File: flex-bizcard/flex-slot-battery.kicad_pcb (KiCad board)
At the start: 2 copper layers, 71.9 x 26.5 mm, 8 parts, among them J1 Conn_01x01_Female, J2 Conn_01x01_Female, J3 Conn_01x01_Female

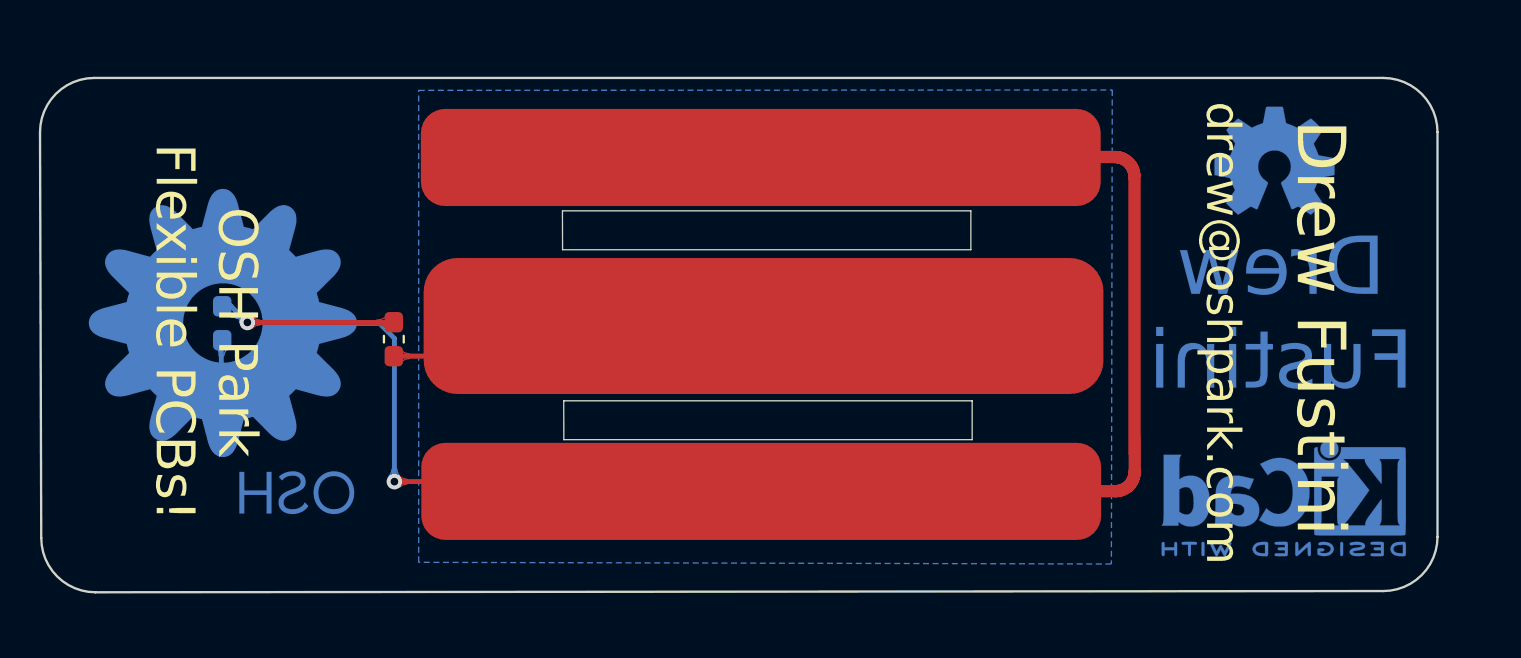
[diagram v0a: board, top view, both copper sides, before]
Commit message: add polarity mark to flex coin slot
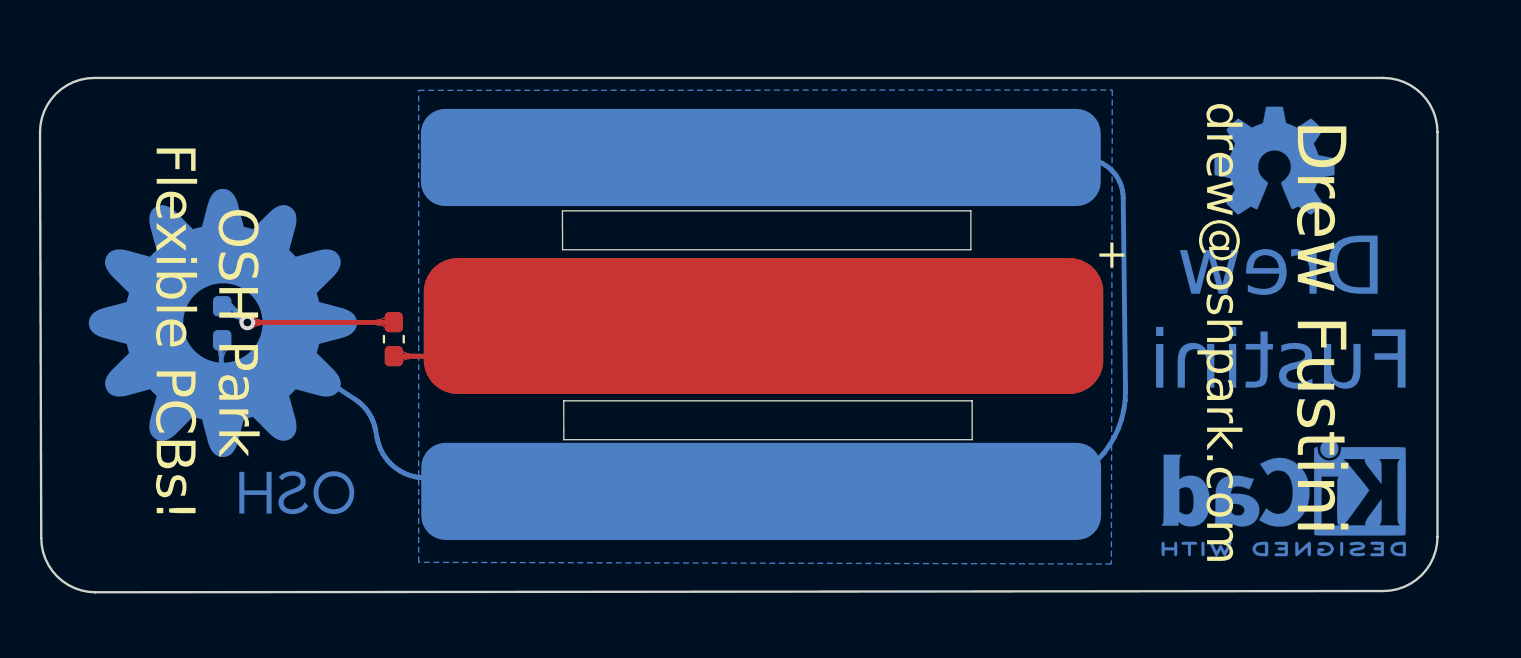
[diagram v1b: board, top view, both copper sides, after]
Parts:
- J2, J3: moved to B.Cu
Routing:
- net GND: track 95.3 -> 87.4 mm, vias 1 -> 0
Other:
- board text added: "+"

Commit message: remove resistors
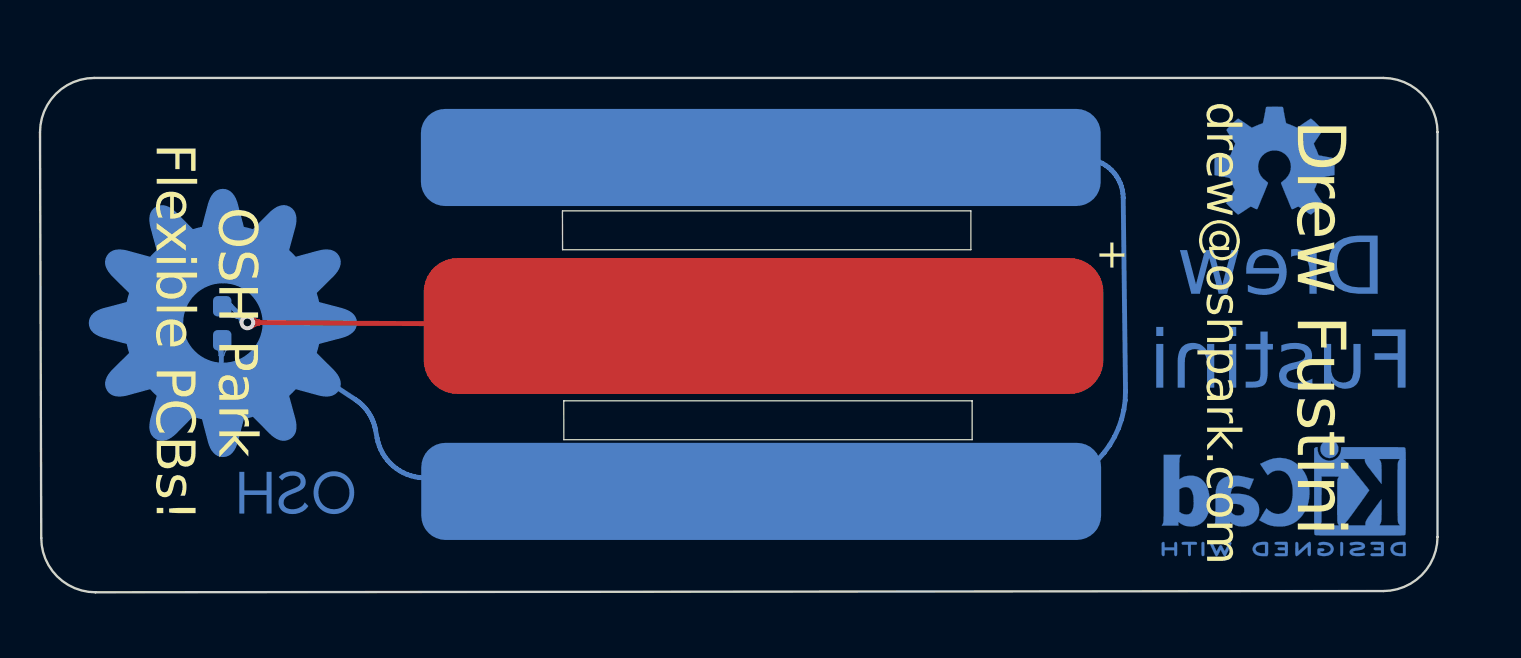
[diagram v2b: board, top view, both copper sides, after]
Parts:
- removed R1: R, afterdark:R_0603_1608Metric_Pad1.05x0.95mm_HandSolder-no-silk
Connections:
- D1 pad 2: Net-(D1-Pad2) -> +3V3
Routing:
- net +3V3: track 19.7 -> 30.5 mm, vias 0 -> 1
- net Net-(D1-Pad2): track 9.21 -> 0.00 mm, vias 1 -> 0
- removed copper zone on B.Cu, net (none)

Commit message: add copper fill zone to flex slot bizcard
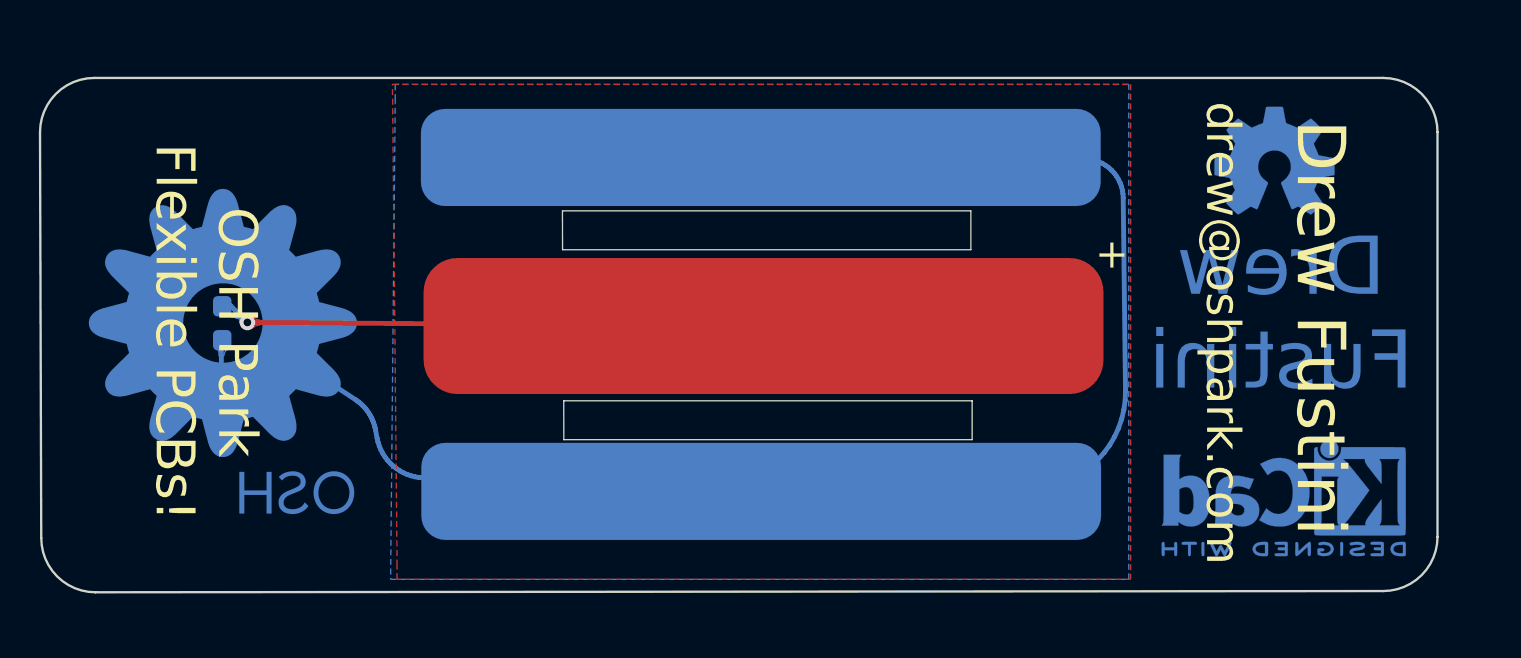
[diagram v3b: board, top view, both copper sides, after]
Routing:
- added copper zone on B.Cu, net (none)
- added copper zone on F.Cu, net (none)
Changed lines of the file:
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@@
+    )
+  )
+  (zone (net 0) (net_name "") (layer F.Cu) (hatch edge 0.508)
+    (connect_pads (clearance 0))
+    (min_thickness 0.254)
+    (fill yes (arc_segments 32) (thermal_gap 0.508) (thermal_bridge_width 0.508))
+    (polygon
+      (pts
+        (xy 174.192021 66.4464) (xy 136.429841 66.4464) (xy 136.429841 65.74028) (xy 136.191081 40.96766) (xy 174.192021 40.96766)
+      )
+    )
+  )
+  (zone (net 0) (net_name "") (layer B.Cu) (hatch edge 0.508)
+    (connect_pads (clearance 0))
+    (min_thickness 0.254)
+    (fill yes (arc_segments 32) (thermal_gap 0.508) (thermal_bridge_width 0.508))
+    (polygon
+      (pts
+        (xy 174.09668 40.975153) (xy 136.3345 40.975153) (xy 136.3345 41.681273) (xy 136.09574 66.453893) (xy 174.09668 66.453893)
+      )
     )
   )
